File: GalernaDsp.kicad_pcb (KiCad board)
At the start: 4 copper layers, 194.5 x 118.5 mm, 119 parts, among them CN100 HX JN1.27-2X5 TP H4.9, J100 DM3CS-SF, J200 Headphones, J201 AudioInput, J202 AudioOutput, J300 USB_C_Receptacle_USB2.0_16P, SW400 100SP1T1B4M2QE, SW401 100SP1T1B4M2QE, U100 SW_RUN, U101 STM32F405RGTx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

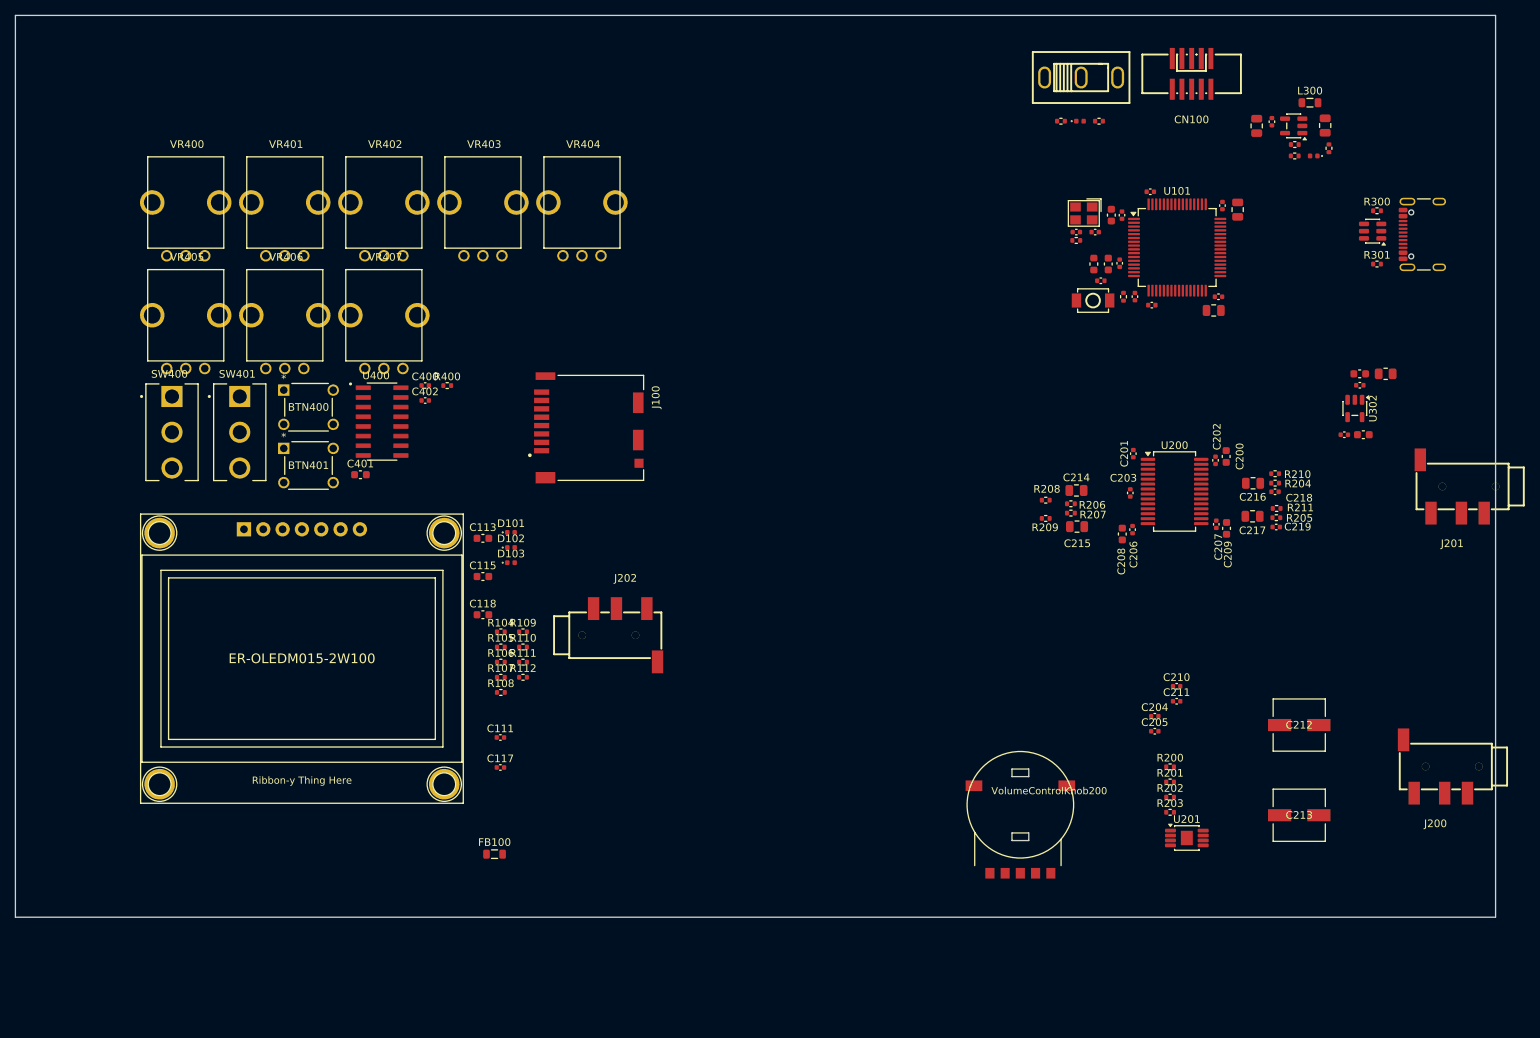
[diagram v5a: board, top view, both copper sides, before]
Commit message: control positioned
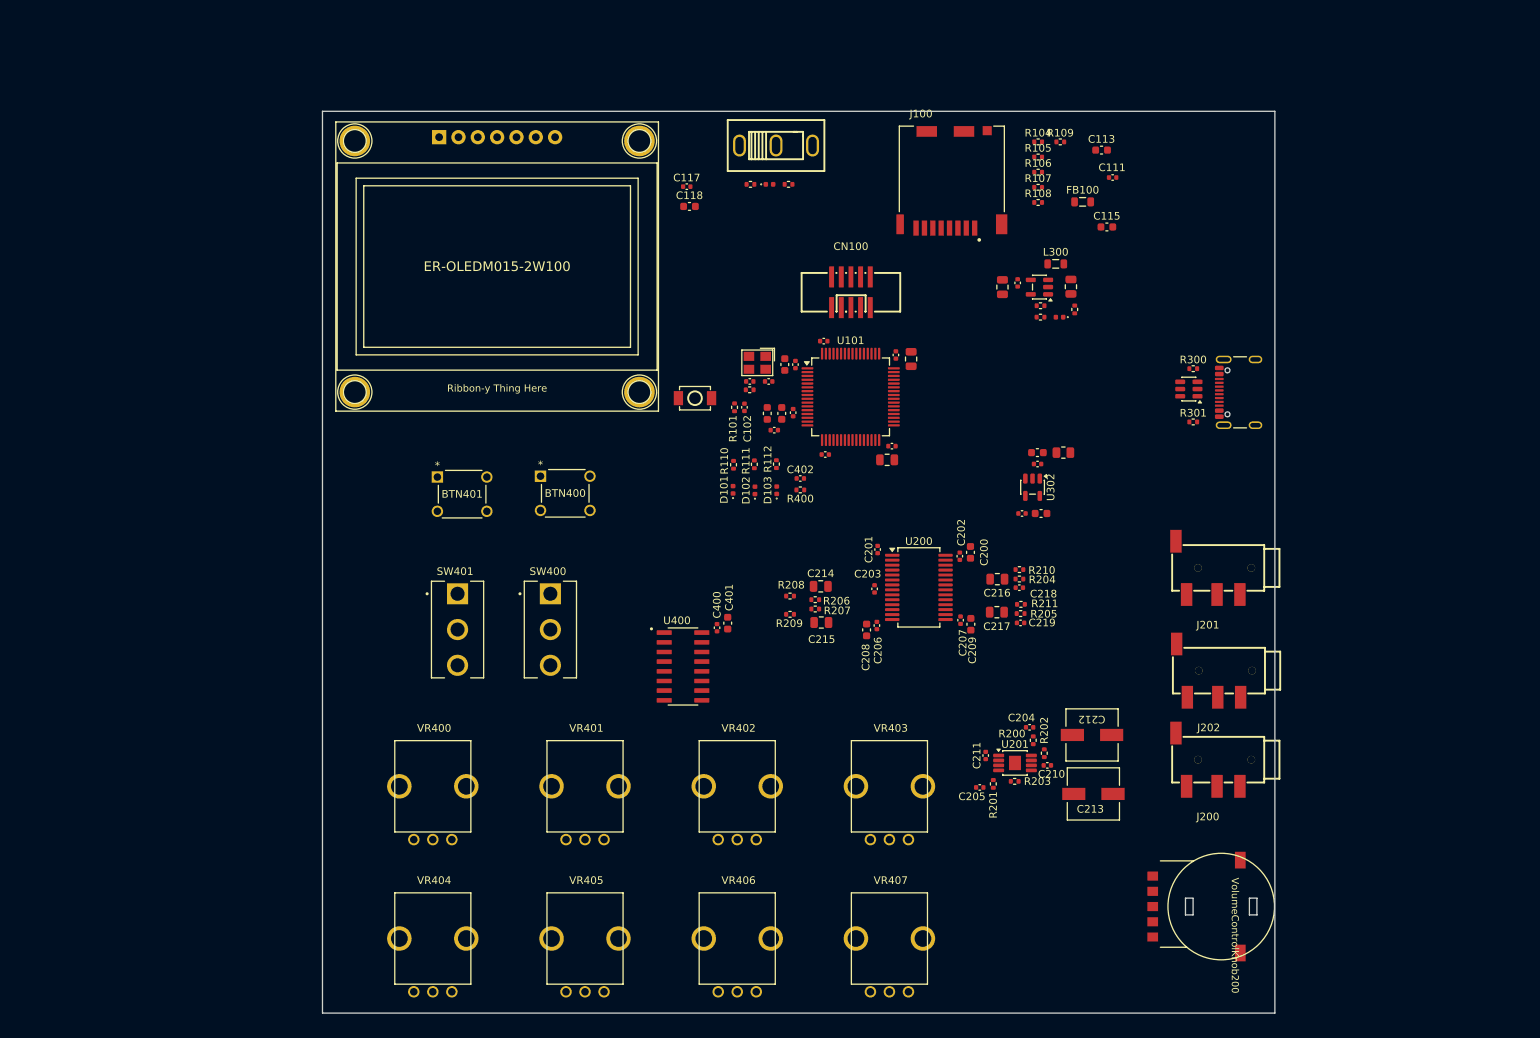
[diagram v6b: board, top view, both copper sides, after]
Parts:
- moved FB100 115.4 mm to (224.7, 47.0)
- moved C111 109.0 mm to (228.7, 43.8)
- moved VR407 105.5 mm to (199.3, 150.8)
- moved VR406 101.2 mm to (179.3, 150.8)
- moved VR404 98.7 mm to (139.3, 150.8)
- moved VR405 97.3 mm to (159.3, 150.8)
- moved C113 96.0 mm to (227.2, 40.2)
- moved R105 95.5 mm to (218.9, 41.1)
- moved R108 95.5 mm to (218.9, 47.1)
- moved R109 95.5 mm to (221.8, 39.1)
- moved R104 95.5 mm to (218.9, 39.1)
- moved R106 95.5 mm to (218.9, 43.1)
- moved R107 95.5 mm to (218.9, 45.1)
- moved C115 94.0 mm to (227.9, 50.3)
- moved VR403 93.5 mm to (199.3, 130.8)
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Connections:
- U101 pad 15: unconnected-(U101-PA1-Pad15) -> /[1] MCU/LED_0
- U101 pad 16: unconnected-(U101-PA2-Pad16) -> /[1] MCU/LED_1
- U101 pad 17: unconnected-(U101-PA3-Pad17) -> /[1] MCU/LED_2
- U101 pad 41: /[1] MCU/LED_2 -> unconnected-(U101-PA8-Pad41)
- U101 pad 42: /[1] MCU/LED_1 -> unconnected-(U101-PA9-Pad42)
- U101 pad 43: /[1] MCU/LED_0 -> unconnected-(U101-PA10-Pad43)
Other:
- board size 194.5 x 118.5 mm -> 125.2 x 118.5 mm

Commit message: updating names
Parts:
- removed VolumeControlKnob200: ~, Galerna:RK10J12R0A0B
- added D104: RCLAMP0521P-N, Galerna:X1-DFN1006-2_L1.0-W0.6-P0.65-BI, F.Cu at (212.7, 36.5)
- added H000: MountingHole, MountingHole:MountingHole_2.5mm, F.Cu at (129.0, 40.0)
- added H001: MountingHole, MountingHole:MountingHole_2.5mm, F.Cu at (245.8, 39.8)
- added H002: MountingHole, MountingHole:MountingHole_2.5mm, F.Cu at (128.2, 150.2)
- added H003: MountingHole, MountingHole:MountingHole_2.5mm, F.Cu at (246.0, 149.8)
- added R212: RK09L12D0A1W, Galerna:RK09L12D0A1W_AAL, F.Cu at (216.5, 150.0)
- moved R104 30.7 mm to (201.4, 64.3), turned to 90 degrees
- moved C118 25.0 mm to (148.7, 41.8), turned to 180 degrees
- moved C117 24.5 mm to (148.7, 40.4), turned to 180 degrees
- moved R109 20.5 mm to (210.1, 55.9), turned to 90 degrees
- moved FB100 20.3 mm to (216.1, 65.3), turned to 180 degrees
- moved C113 19.5 mm to (208.1, 36.4), turned to 180 degrees
- moved C111 19.3 mm to (210.8, 36.5), turned to 180 degrees
- moved C115 17.2 mm to (219.6, 65.3)
- moved R105 16.1 mm to (212.8, 55.9), turned to 90 degrees
- moved R108 14.4 mm to (207.6, 55.9), turned to 90 degrees
- moved R106 13.3 mm to (215.2, 55.9), turned to 90 degrees
- moved SW_100 12.9 mm to (185.3, 78.7)
- moved L300 11.0 mm to (223.9, 65.8)
- moved R107 10.9 mm to (217.8, 55.9), turned to 90 degrees
- moved C300 10.6 mm to (217.9, 68.2)
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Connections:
- net /[1] MCU/MCU_SDIO_CK renamed /[1] MCU/SDCARD_SDIO_CK
- net /[1] MCU/MCU_SDIO_CMD renamed /[1] MCU/SDCARD_SDIO_CMD
- net /[1] MCU/MCU_SDIO_D0 renamed /[1] MCU/SDCARD_SDIO_D0
- net /[1] MCU/MCU_SDIO_D1 renamed /[1] MCU/SDCARD_SDIO_D1
- net /[1] MCU/MCU_SDIO_D2 renamed /[1] MCU/SDCARD_SDIO_D2
- net /[1] MCU/MCU_SDIO_D3 renamed /[1] MCU/SDCARD_SDIO_D3
- net /[1] MCU/SD_CARD_DETECT renamed /[1] MCU/SDCARD_DETECT
- net I2C_SCL renamed CODEC_I2C_SCL
- net I2C_SDA renamed CODEC_I2C_SDA
- net I2S_CK renamed CODEC_I2S_CK
- net I2S_MCK renamed CODEC_I2S_MCK
- net I2S_SD renamed CODEC_I2S_SD
- net I2S_SDI renamed CODEC_I2S_SDI
- net I2S_WS renamed CODEC_I2S_WS

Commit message: net classes added
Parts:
- H000, H001, H002, H003: footprint MountingHole:MountingHole_2.5mm -> MountingHole:MountingHole_3.2mm_M3_DIN965_Pad_TopBottom
- moved BTN401 19.1 mm to (163.0, 90.0)
- moved BTN400 18.6 mm to (143.0, 90.0)
- moved H003 7.00 mm to (239.0, 150.0)
- moved H001 6.75 mm to (239.0, 40.0)
- moved J202 5.81 mm to (236.9, 104.8)
- moved J200 5.81 mm to (236.8, 116.5)
- moved J201 5.81 mm to (236.8, 91.3)
- moved J300 4.97 mm to (241.4, 72.4)
- moved R300 4.62 mm to (234.7, 69.3)
- moved R301 4.62 mm to (234.7, 76.3)
- moved U300 4.62 mm to (234.1, 72.0)
- moved C300 3.51 mm to (219.5, 65.0)
- moved C302 3.51 mm to (217.5, 65.5)
- moved C306 3.51 mm to (226.5, 65.5)
- moved D300 3.51 mm to (225.0, 69.5)
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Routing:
- net +3V3: track 0.00 -> 5.40 mm
- net Net-(U101-VCAP_2): track 0.00 -> 2.37 mm
- net GND: track 0.00 -> 2.08 mm
- added copper zone on F.Cu, net +3V3
- added copper zone on F.Cu, net GND
- added copper zone on In1.Cu, net GND
- added copper zone on In2.Cu, net GND
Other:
- board size 125.2 x 118.5 mm -> 121 x 121 mm
